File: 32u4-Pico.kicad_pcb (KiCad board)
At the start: 2 copper layers, 21.3 x 51.3 mm, 25 parts, among them J3 2.54mm header 01x20, J4 2.54mm header 01x20, U1 ATmega32U4-MU, Y1 8MHz 3225_4p crystal

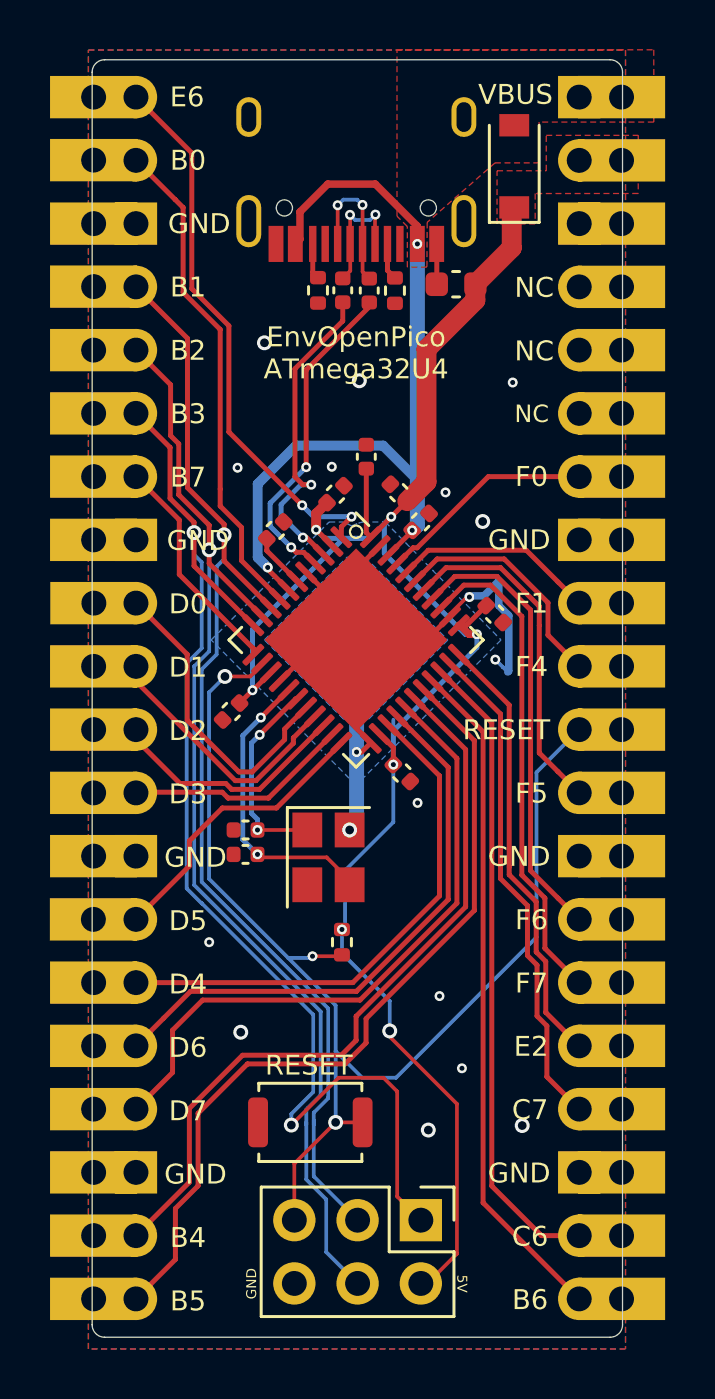
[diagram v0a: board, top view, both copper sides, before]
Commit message: added correct orientation USB TP Pads to match RPI PICO and my Pico clone
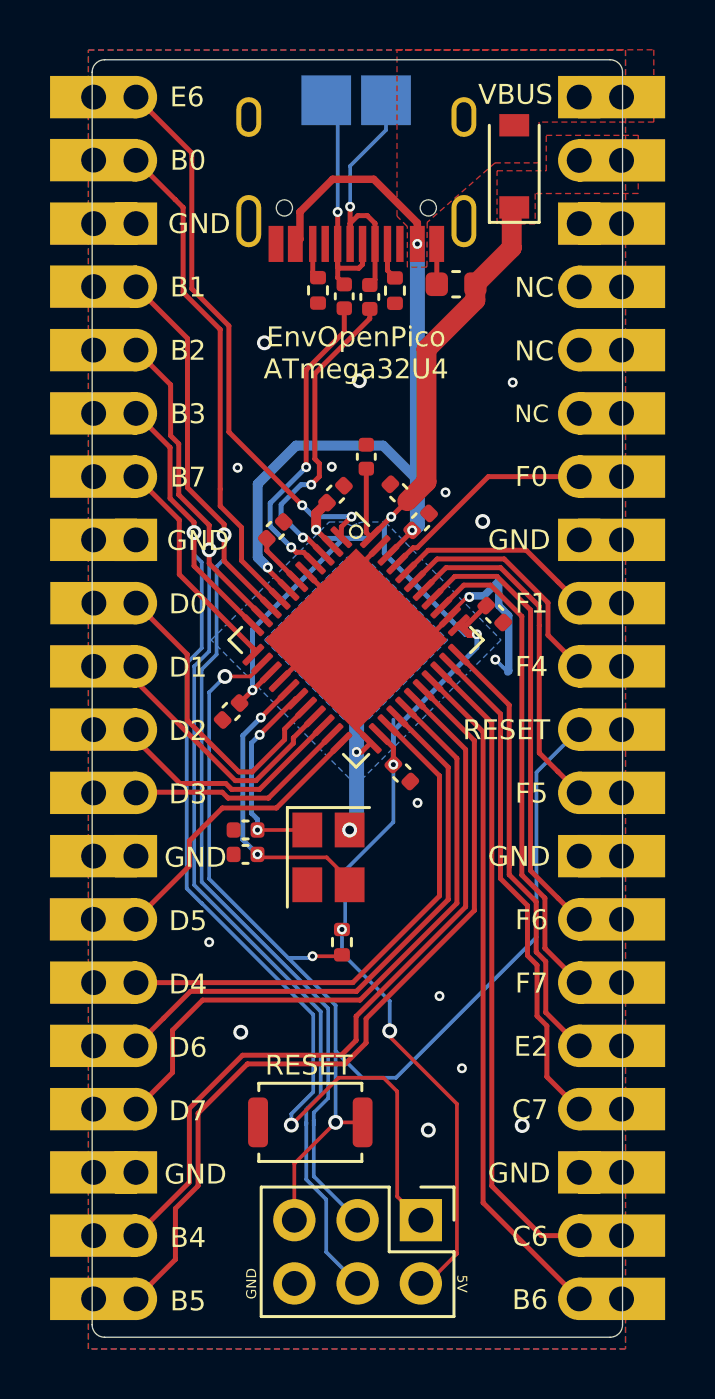
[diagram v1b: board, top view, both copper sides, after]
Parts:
- added TP1: TestPoint, TestPoint:TestPoint_Pad_2.0x2.0mm, B.Cu at (102.4, 58.9)
- added TP2: TestPoint, TestPoint:TestPoint_Pad_2.0x2.0mm, B.Cu at (104.8, 58.9)
- moved R4 1.12 mm to (104.1, 66.8)
- moved R3 1.03 mm to (103.1, 66.7)
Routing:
- net USB_D-: track 4.89 -> 11.0 mm, vias 2 -> 1
- net USB_D+: track 5.80 -> 11.3 mm, vias 2 -> 1
- net Net-(R3-Pad2): track 13.1 -> 12.4 mm
